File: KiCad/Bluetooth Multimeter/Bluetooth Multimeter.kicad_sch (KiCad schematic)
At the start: 30 parts, among them J1 V/Ohm, J2 Com, J3 mA, J4 A, J5 Parallel Prot, K1 Low Range, K2 Medium Range, K3 High Range, K4 UH Range (Ohm Only), K5 V/Ohm Switch, U1 ItsyBitsy_NRF52840_Big

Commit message: Slightly Modifided PCB
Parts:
- added D9: 1N4148, Diode_THT:D_DO-35_SOD27_P7.62mm_Horizontal, symbol Diode:1N4148
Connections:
- net GND: now also D9.2 (A)
- net V/Ohm Control: now also D9.1 (K)
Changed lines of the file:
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@@
   (junction (at 120.015 123.19) (diameter 0) (color 0 0 0 0)
   )
+  (junction (at 83.82 143.51) (diameter 0) (color 0 0 0 0)
+  )
   (junction (at 136.525 153.035) (diameter 0) (color 0 0 0 0)
   )
@@
   )
   (junction (at 120.015 26.67) (diameter 0) (color 0 0 0 0)
+  )
+  (junction (at 92.71 143.51) (diameter 0) (color 0 0 0 0)
   )
   (junction (at 120.015 58.42) (diameter 0) (color 0 0 0 0)
@@
     (stroke (width 0) (type default))
   )
+  (wire (pts (xy 91.44 143.51) (xy 92.71 143.51))
+    (stroke (width 0) (type default))
+  )
   (wire (pts (xy 95.25 99.06) (xy 93.98 99.06))
     (stroke (width 0) (type default))
@@
     (stroke (width 0) (type default))
   )
+  (wire (pts (xy 83.82 143.51) (xy 85.09 143.51))
+    (stroke (width 0) (type default))
+  )
   (wire (pts (xy 231.775 104.14) (xy 231.775 111.76))
     (stroke (width 0) (type default))
@@
     (stroke (width 0) (type default))
   )
-  (wire (pts (xy 96.52 140.97) (xy 92.075 140.97))
+  (wire (pts (xy 96.52 140.97) (xy 83.82 140.97))
     (stroke (width 0) (type default))
   )
@@
     (stroke (width 0) (type default))
   )
-  (wire (pts (xy 90.805 138.43) (xy 93.98 138.43))
+  (wire (pts (xy 80.01 138.43) (xy 93.98 138.43))
     (stroke (width 0) (type default))
   )
@@
     (stroke (width 0) (type default))
   )
-  (wire (pts (xy 92.075 150.495) (xy 140.335 150.495))
+  (wire (pts (xy 83.82 150.495) (xy 140.335 150.495))
     (stroke (width 0) (type default))
   )
@@
     (stroke (width 0) (type default))
   )
-  (wire (pts (xy 90.805 156.21) (xy 90.805 138.43))
+  (wire (pts (xy 80.01 156.21) (xy 80.01 138.43))
     (stroke (width 0) (type default))
   )
@@
     (stroke (width 0) (type default))
   )
-  (wire (pts (xy 90.805 156.21) (xy 146.05 156.21))
+  (wire (pts (xy 80.01 156.21) (xy 146.05 156.21))
     (stroke (width 0) (type default))
   )
@@
     (stroke (width 0) (type default))
   )
+  (wire (pts (xy 92.71 144.78) (xy 92.71 143.51))
+    (stroke (width 0) (type default))
+  )
   (wire (pts (xy 156.845 85.09) (xy 163.195 85.09))
     (stroke (width 0) (type default))
@@
     (stroke (width 0) (type default))
   )
+  (wire (pts (xy 83.82 143.51) (xy 83.82 150.495))
+    (stroke (width 0) (type default))
+  )
   (wire (pts (xy 199.39 92.71) (xy 191.135 92.71))
     (stroke (width 0) (type default))
@@
     (stroke (width 0) (type default))
   )
-  (wire (pts (xy 95.25 143.51) (xy 96.52 143.51))
+  (wire (pts (xy 92.71 143.51) (xy 96.52 143.51))
     (stroke (width 0) (type default))
   )
@@
     (stroke (width 0) (type default))
   )
-  (wire (pts (xy 92.075 140.97) (xy 92.075 150.495))
+  (wire (pts (xy 83.82 140.97) (xy 83.82 143.51))
     (stroke (width 0) (type default))
   )
@@
         (path "/af47cb4a-7c1c-4e81-945f-98b3452c887a"
           (reference "#PWR09") (unit 1)
+        )
+      )
+    )
+  )
+  (symbol (lib_id "Diode:1N4148") (at 87.63 143.51 0) (unit 1)
+    (in_bom yes) (on_board yes) (dnp no)
+    (property "Reference" "D9" (at 83.82 142.24 0)
+      (effects (font (size 1.27 1.27)) (justify left))
+    )
+    (property "Value" "1N4148" (at 83.82 146.05 0)
+      (effects (font (size 1.27 1.27)) (justify left))
+    )
+    (property "Footprint" "Diode_THT:D_DO-35_SOD27_P7.62mm_Horizontal" (at 87.63 143.51 0)
+      (effects (font (size 1.27 1.27)) hide)
+    )
+    (property "Datasheet" "https://assets.nexperia.com/documents/data-sheet/1N4148_1N4448.pdf" (at 87.63 143.51 0)
+      (effects (font (size 1.27 1.27)) hide)
+    )
+    (property "Sim.Device" "D" (at 87.63 143.51 0)
+      (effects (font (size 1.27 1.27)) hide)
+    )
+    (property "Sim.Pins" "1=K 2=A" (at 87.63 143.51 0)
+      (effects (font (size 1.27 1.27)) hide)
+    )
+    (pin "1")
+    (pin "2")
+    (instances
+      (project "Bluetooth Multimeter"
+        (path "/9883bcc4-8e34-47d7-83c1-7917e414ffa8"
+          (reference "D9") (unit 1)
+        )
+      )
+      (project "BTMM Recovery"
+        (path "/af47cb4a-7c1c-4e81-945f-98b3452c887a"
+          (reference "D8") (unit 1)
         )
       )
@@
     )
   )
-  (symbol (lib_id "power:GND") (at 95.25 143.51 270) (unit 1)
-    (in_bom yes) (on_board yes) (dnp no)
-    (property "Reference" "#PWR08" (at 88.9 143.51 0)
-      (effects (font (size 1.27 1.27)) hide)
-    )
-    (property "Value" "GND" (at 96.52 142.24 90)
+  (symbol (lib_id "power:GND") (at 92.71 144.78 0) (unit 1)
+    (in_bom yes) (on_board yes) (dnp no)
+    (property "Reference" "#PWR08" (at 92.71 151.13 0)
+      (effects (font (size 1.27 1.27)) hide)
+    )
+    (property "Value" "GND" (at 92.71 149.86 0)
       (effects (font (size 1.27 1.27)))
     )
-    (property "Footprint" "" (at 95.25 143.51 0)
-      (effects (font (size 1.27 1.27)) hide)
-    )
-    (property "Datasheet" "" (at 95.25 143.51 0)
-      (effects (font (size 1.27 1.27)) hide)
-    )
+    (property "Footprint" "" (at 92.71 144.78 0)
+      (effects (font (size 1.27 1.27)) hide)
+    )
+    (property "Datasheet" "" (at 92.71 144.78 0)
+      (effects (font (size 1.27 1.27)) hide)
+    )

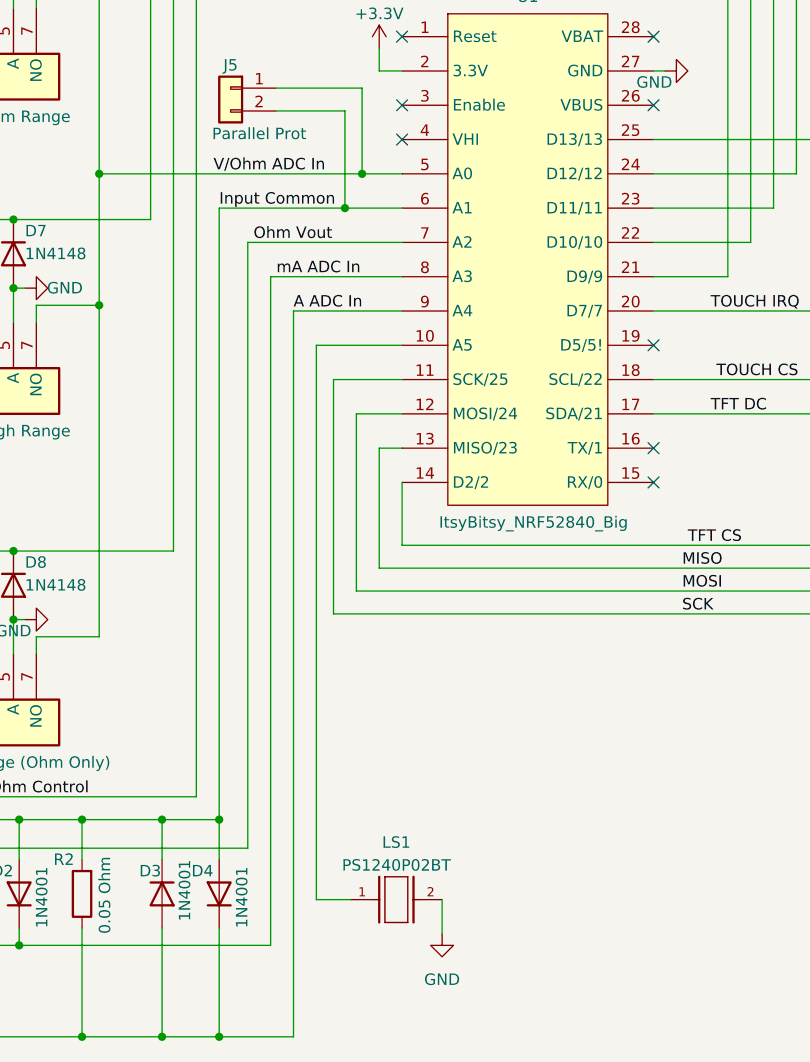
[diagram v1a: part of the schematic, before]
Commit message: began main arduino project, modified KiCad itsybitsy symbol
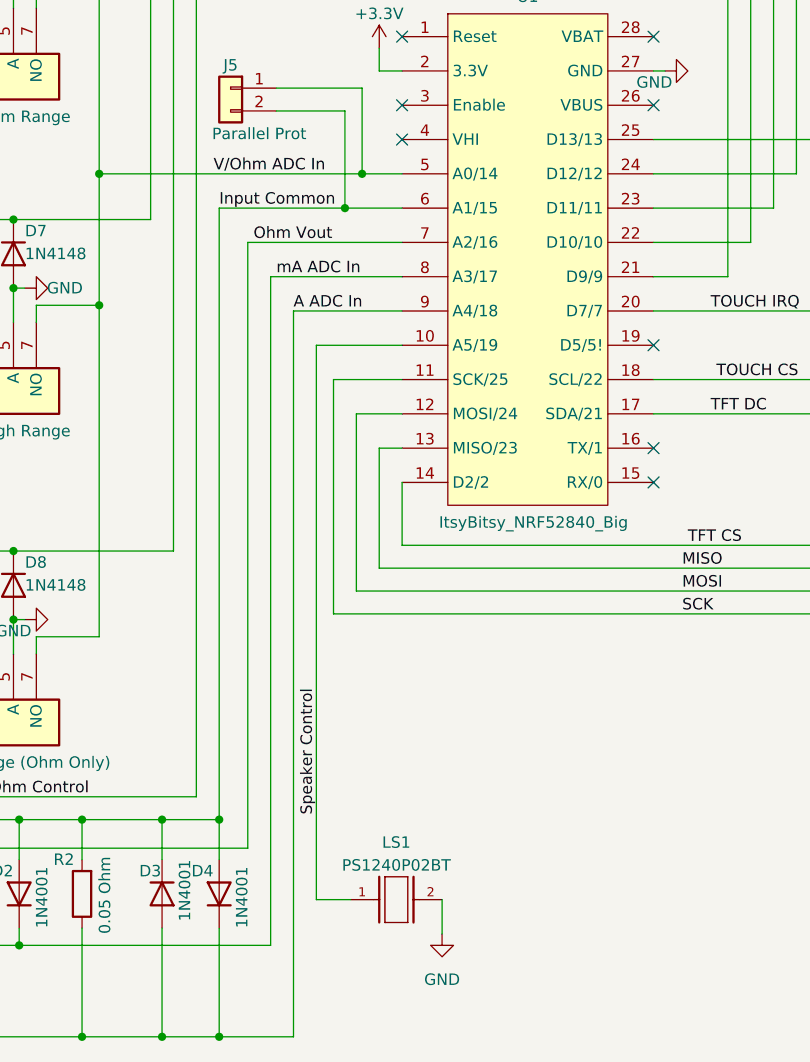
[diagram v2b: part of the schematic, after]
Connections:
- net Speaker Control: now reaches LS1.1, U1., U1.10 (A5/19)
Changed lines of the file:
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@@
     (stroke (width 0) (type default))
   )
-  (wire (pts (xy 153.67 161.925) (xy 153.67 100.33))
+  (wire (pts (xy 153.67 100.33) (xy 153.67 161.925))
     (stroke (width 0) (type default))
   )
@@
     (effects (font (size 1.27 1.27)) (justify left bottom))
   )
+  (label "Speaker Control" (at 153.67 138.43 270) (fields_autoplaced)
+    (effects (font (size 1.27 1.27)) (justify right bottom))
+  )
   (label "V{slash}Ohm Control" (at 115.57 150.495 0) (fields_autoplaced)
